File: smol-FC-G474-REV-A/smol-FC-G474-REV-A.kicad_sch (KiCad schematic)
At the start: 0 parts

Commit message: Schematic update
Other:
- added sheet Sensors & IC's (sens%IC.kicad_sch)
- sheet MCU ports: added ADC_CURR, AUX, Buzzer, CC, I2C3_SCL, I2C3_SDA, I2C4_SCL (BARO), I2C4_SDA (BARO), IMU_IRQ, LED, M1, M2, M3, M4, RX1, RX2 (VTX), RX3 (ELRS), RX4 (GPS), RX5 (TEL), SPI1_CS (OSD), SPI1_MISO (OSD), SPI1_MOSI (OSD), SPI1_SCK (OSD), SPI2_CS (IMU), SPI2_MISO (IMU), SPI2_MOSI (IMU), SPI2_SCK (IMU), SPI3_CS (Blackbox), SPI3_MISO (Blackbox), SPI3_MOSI (Blackbox), SPI3_SCK (Blackbox), TX1, TX2 (VTX), TX3 (ELRS), TX4 (GPS), TX5 (TEL); removed none

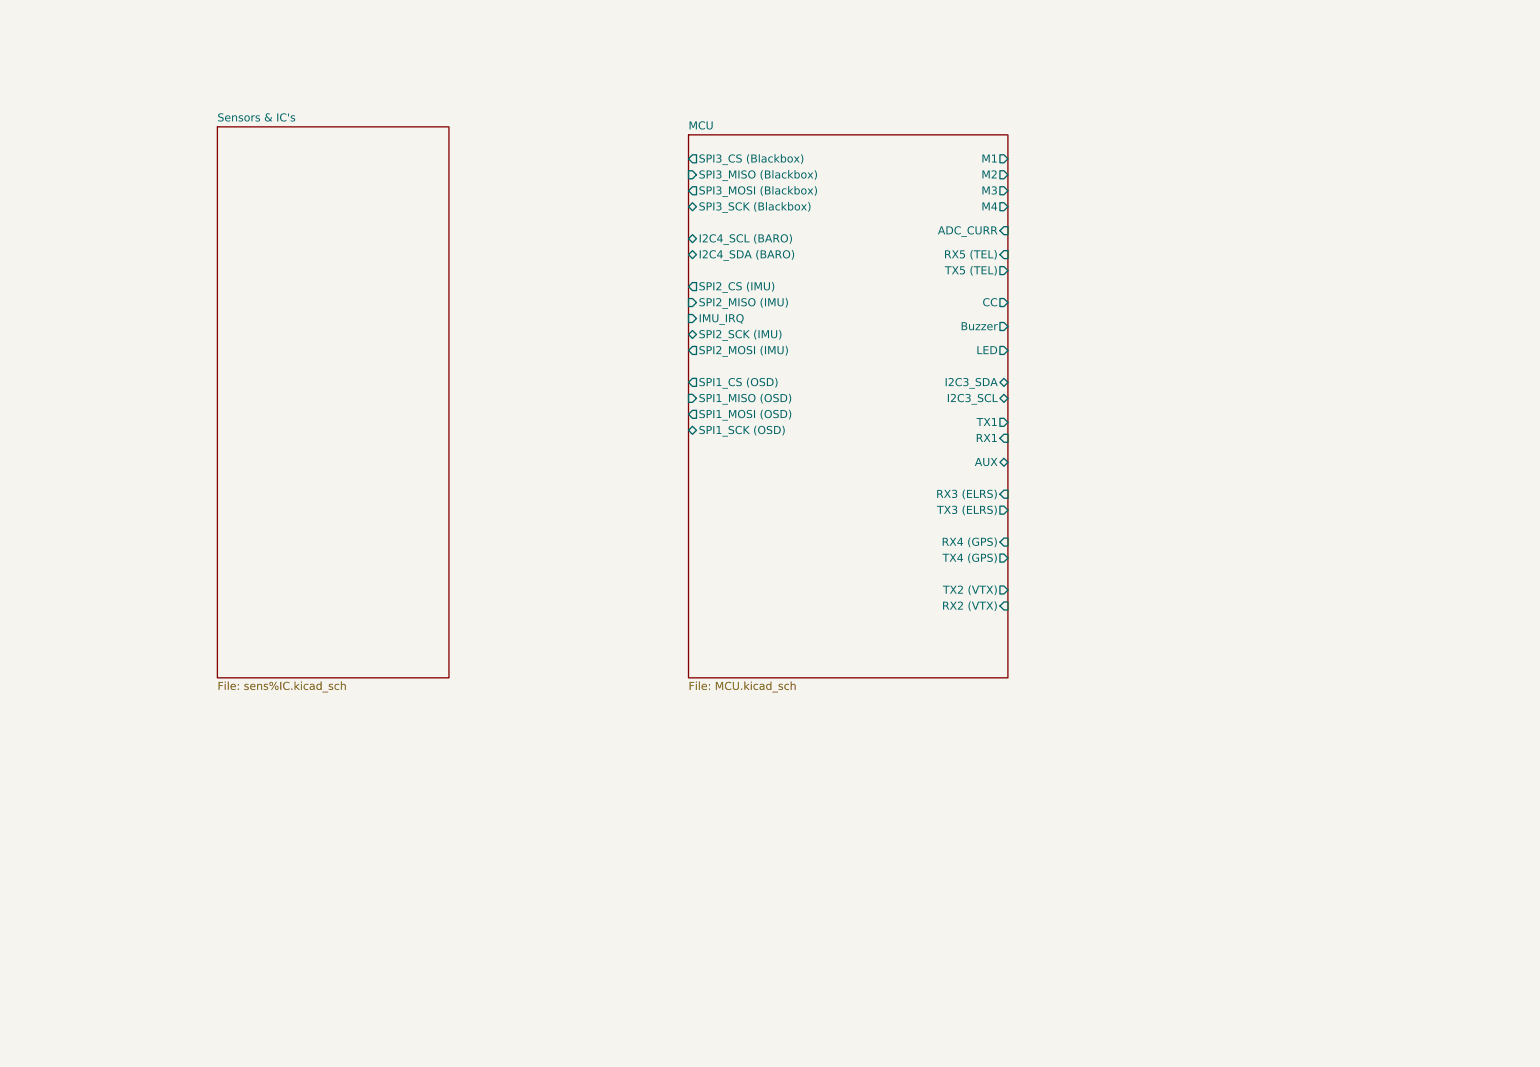
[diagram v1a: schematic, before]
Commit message: Added whole new schematic (sensors, OSD, Blackbox), changed text in cubemx
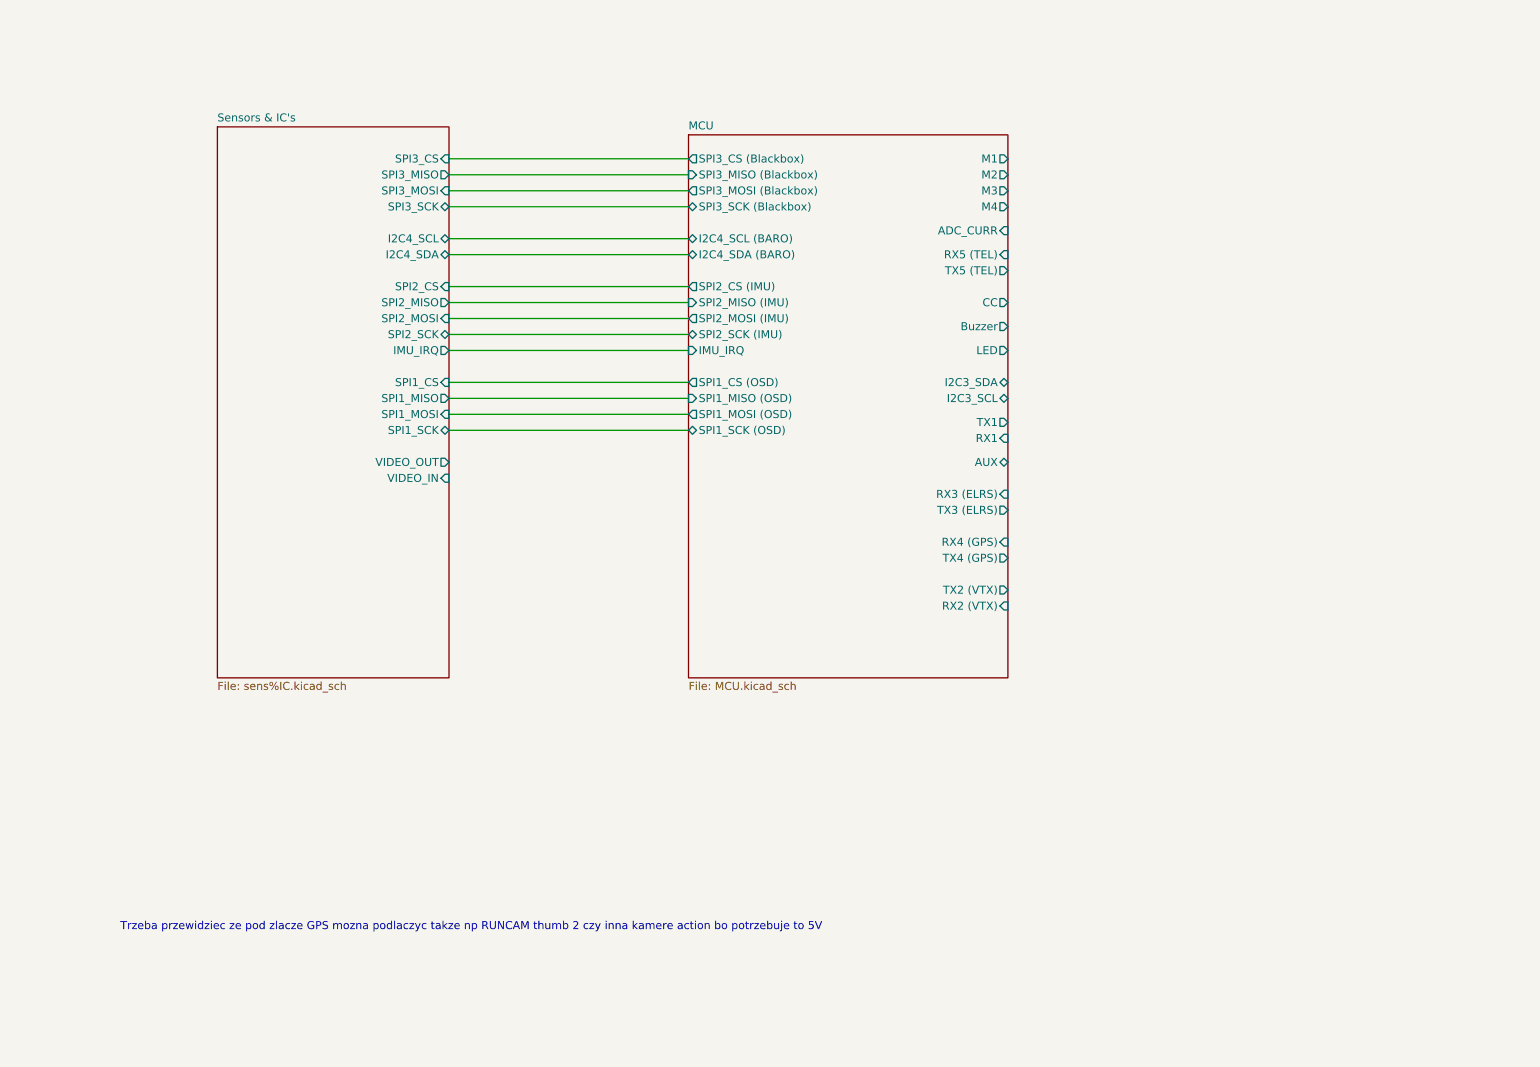
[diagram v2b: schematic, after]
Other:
- sheet Sensors & IC's ports: added I2C4_SCL, I2C4_SDA, IMU_IRQ, SPI1_CS, SPI1_MISO, SPI1_MOSI, SPI1_SCK, SPI2_CS, SPI2_MISO, SPI2_MOSI, SPI2_SCK, SPI3_CS, SPI3_MISO, SPI3_MOSI, SPI3_SCK, VIDEO_IN, VIDEO_OUT; removed none
- note added: "Trzeba przewidziec ze pod zlacze GPS mozna podlaczyc takze np RUNCAM thumb 2 czy inna kamere action bo potrzebuje to 5V"

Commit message: complete connectors layout and initialize buck converter section. Added buck docs in /docs.
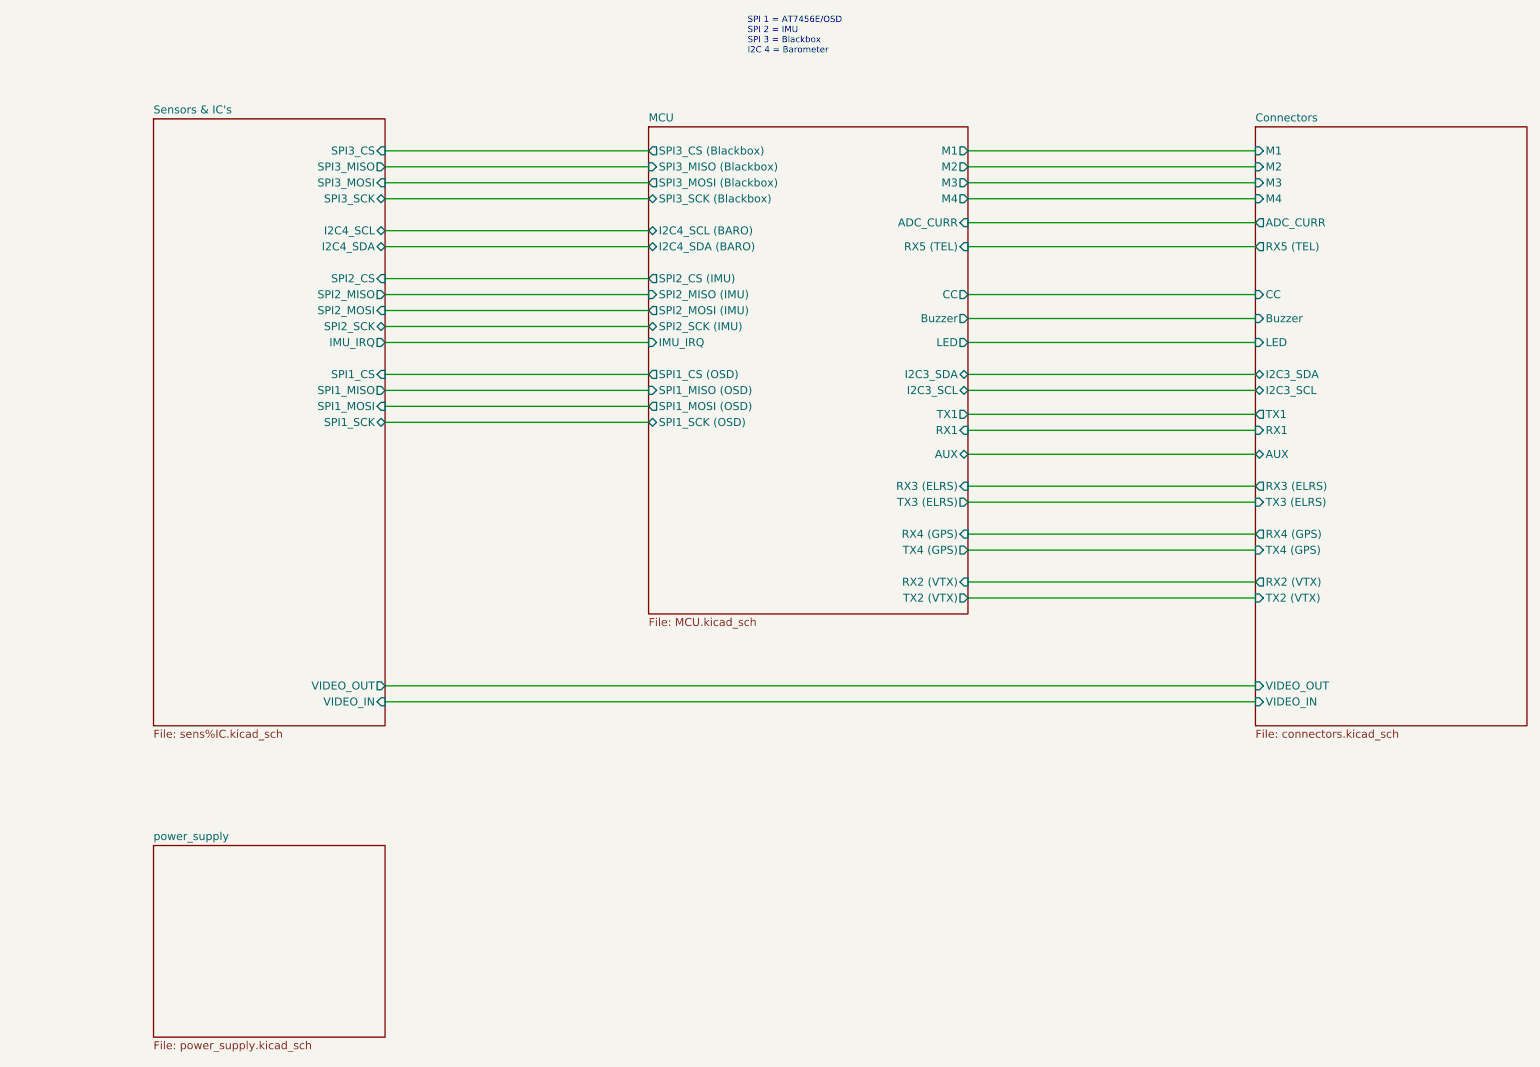
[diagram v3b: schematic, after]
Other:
- added sheet Connectors (connectors.kicad_sch)
- added sheet power_supply (power_supply.kicad_sch)
- sheet MCU ports: added none; removed TX5 (TEL)
- note added: "SPI 1 = AT7456E/OSD SPI 2 = IMU SPI 3 = Blackbox I2C 4 = Barometer"
- note removed: "Trzeba przewidziec ze pod zlacze GPS mozna podlaczyc takze np RUNCAM thumb 2 czy inna kamere action bo potrzebuje to 5V"

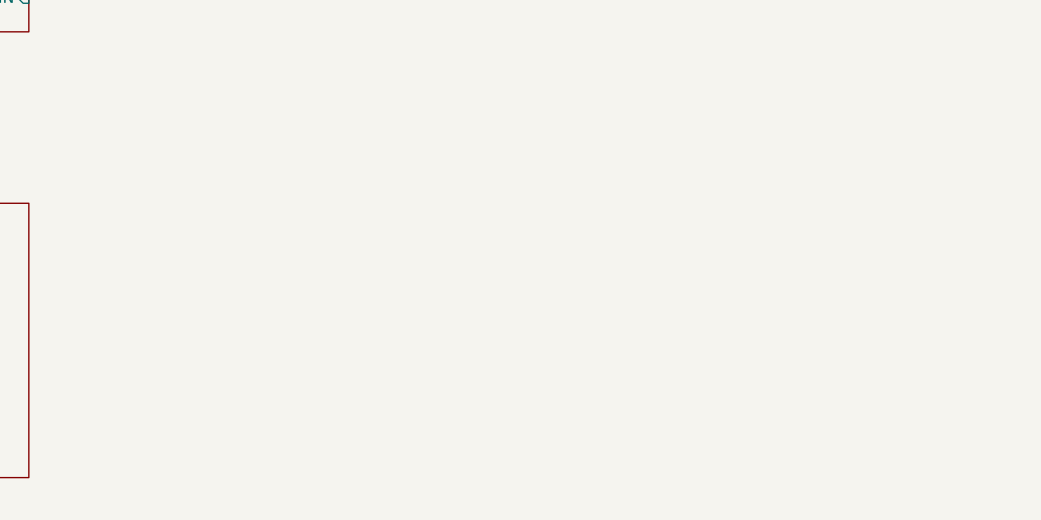
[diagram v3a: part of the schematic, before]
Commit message: Attached footprints and finalized schematic.
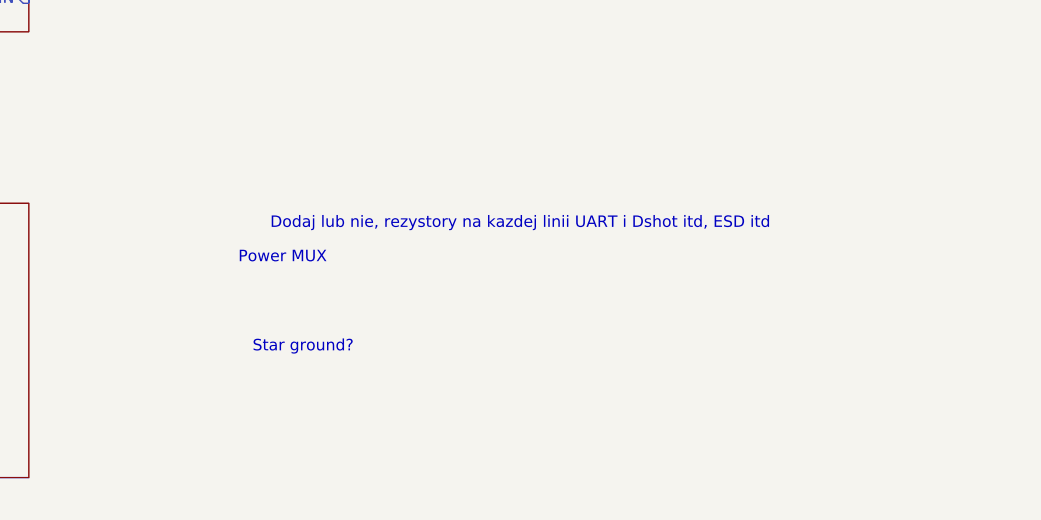
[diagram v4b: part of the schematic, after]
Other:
- note added: "Dodaj lub nie, rezystory na kazdej linii UART i Dshot itd, ESD itd"
- note added: "Power MUX"
- note added: "Star ground?"
- title: smol-FC-G474 -> smol-FC-G474-REV-A
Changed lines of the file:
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@@
 	(paper "A4")
 	(title_block
-		(title "smol-FC-G474")
-		(date "2026-05-31")
-		(rev "0.7.0")
+		(title "smol-FC-G474-REV-A")
+		(date "2026-06-05")
+		(rev "0.9.3")
 		(company "Daniel Plewa")
 		(comment 1 "License: CERN-OHL-W v2")
 		(comment 2 "GitHub: https://github.com/Def12345678/smol-FC-G474-REV-A")
-		(comment 3 "BEC 5A/2A, 10V/2A | Baro, OSD Chip and 16MB blackbox")
+		(comment 3 "BEC 5A/3A, 10V/3A | Baro, OSD Chip and 16MB blackbox")
 		(comment 4 "Open source flight controller on STM32G4, 20x20 3.5mm hole")
 	)
+	(text "Dodaj lub nie, rezystory na kazdej linii UART i Dshot itd, ESD itd"
+		(exclude_from_sim no)
+		(at 133.35 155.956 0)
+		(effects
+			(font
+				(size 1.27 1.27)
+			)
+		)
+	)
+	(text "Power MUX"
+		(exclude_from_sim no)
+		(at 106.934 159.766 0)
+		(effects
+			(font
+				(size 1.27 1.27)
+			)
+		)
+	)
+	(text "Star ground?"
+		(exclude_from_sim no)
+		(at 109.22 169.672 0)
+		(effects
+			(font
+				(size 1.27 1.27)
+			)
+		)
+	)
 	(text "SPI 1 = AT7456E/OSD\nSPI 2 = IMU\nSPI 3 = Blackbox\nI2C 4 = Barometer"

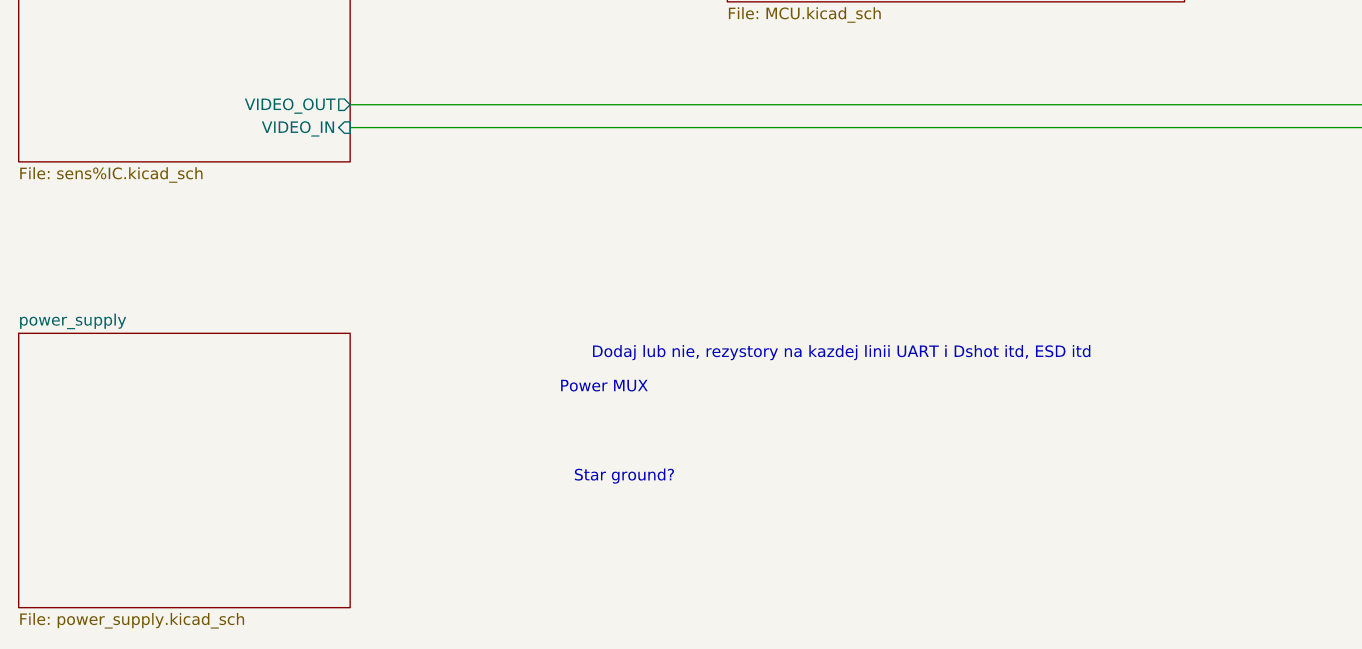
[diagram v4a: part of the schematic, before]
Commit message: Finalized schematic, added power mux
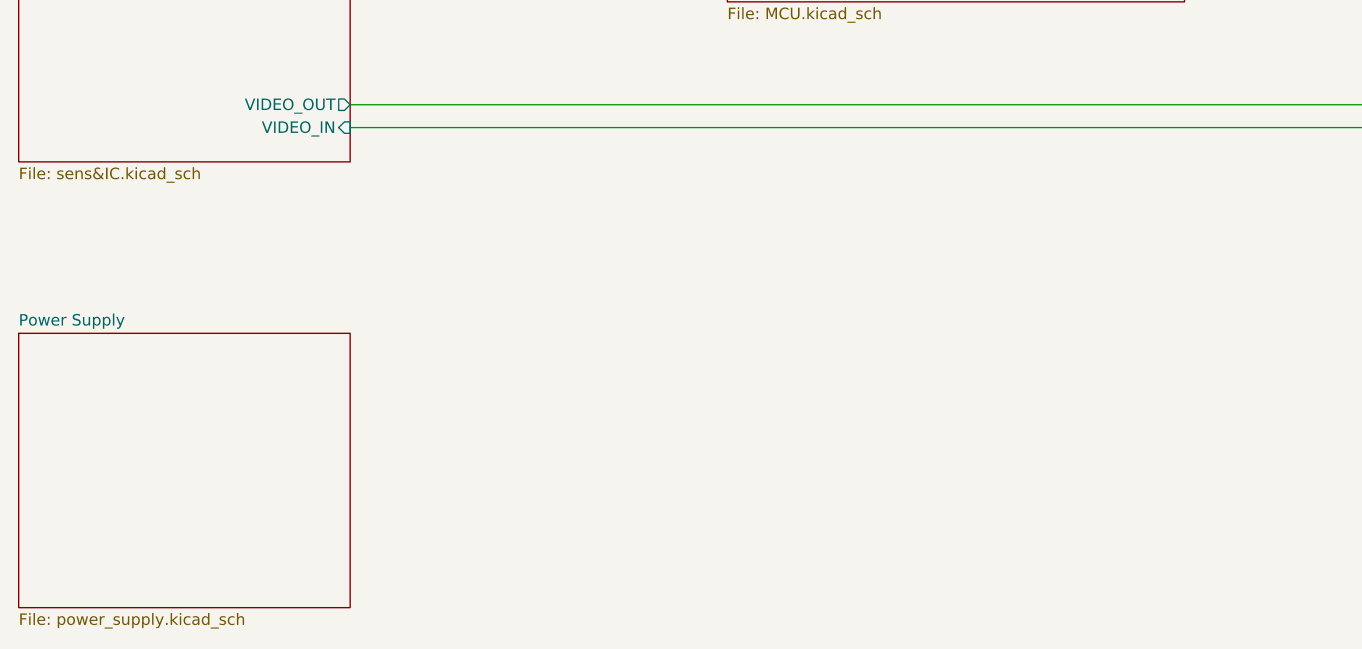
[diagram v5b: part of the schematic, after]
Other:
- sheet power_supply renamed Power Supply
- sheet Sensors & IC's: file sens%IC.kicad_sch -> sens&IC.kicad_sch
- note removed: "Dodaj lub nie, rezystory na kazdej linii UART i Dshot itd, ESD itd"
- note removed: "Power MUX"
- note removed: "Star ground?"
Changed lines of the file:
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@@
 		(comment 1 "License: CERN-OHL-W v2")
 		(comment 2 "GitHub: https://github.com/Def12345678/smol-FC-G474-REV-A")
-		(comment 3 "BEC 5A/3A, 10V/3A | Baro, OSD Chip and 16MB blackbox")
+		(comment 3 "BEC 5A/3A, 9V/3A | Baro, OSD Chip and 16MB blackbox")
 		(comment 4 "Open source flight controller on STM32G4, 20x20 3.5mm hole")
-	)
-	(text "Dodaj lub nie, rezystory na kazdej linii UART i Dshot itd, ESD itd"
-		(exclude_from_sim no)
-		(at 133.35 155.956 0)
-		(effects
-			(font
-				(size 1.27 1.27)
-			)
-		)
-	)
-	(text "Power MUX"
-		(exclude_from_sim no)
-		(at 106.934 159.766 0)
-		(effects
-			(font
-				(size 1.27 1.27)
-			)
-		)
-	)
-	(text "Star ground?"
-		(exclude_from_sim no)
-		(at 109.22 169.672 0)
-		(effects
-			(font
-				(size 1.27 1.27)
-			)
-		)
 	)
 	(text "SPI 1 = AT7456E/OSD\nSPI 2 = IMU\nSPI 3 = Blackbox\nI2C 4 = Barometer"
@@
 			(color 255 229 191 1)
 		)
-		(property "Sheetname" "power_supply"
+		(property "Sheetname" "Power Supply"
 			(at 41.91 152.9584 0)
 			(show_name no)
@@
 			)
 		)
-		(property "Sheetfile" "sens%IC.kicad_sch"
+		(property "Sheetfile" "sens&IC.kicad_sch"
 			(at 41.91 135.2046 0)
 			(show_name no)

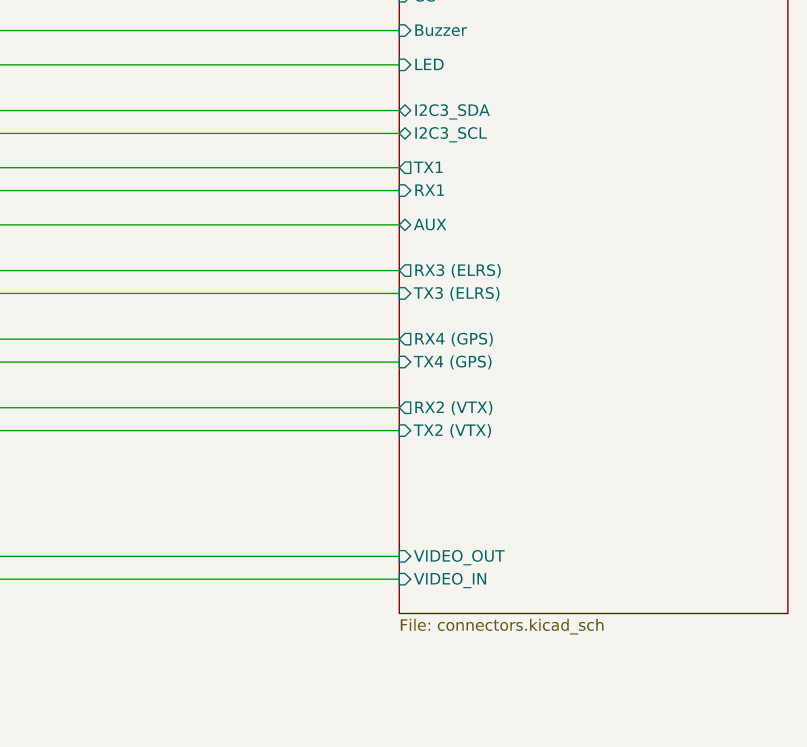
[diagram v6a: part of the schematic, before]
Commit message: changed size of cap on buck's
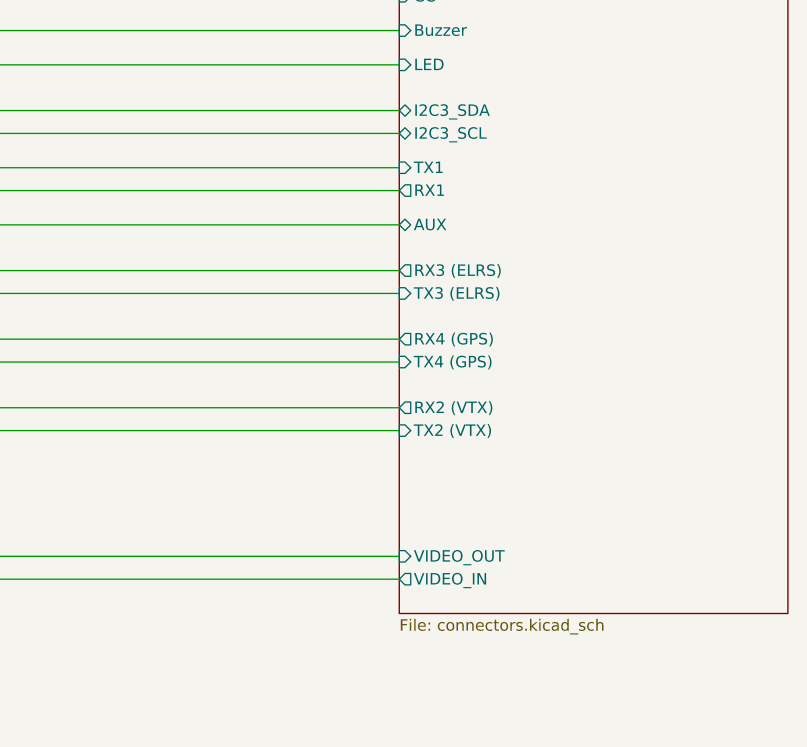
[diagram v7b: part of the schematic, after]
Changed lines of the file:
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@@
 			)
 		)
-		(pin "TX1" output
+		(pin "TX1" input
 			(at 217.17 85.09 180)
 			(effects
@@
 			)
 		)
-		(pin "RX1" input
+		(pin "RX1" output
 			(at 217.17 87.63 180)
 			(effects
@@
 			)
 		)
-		(pin "VIDEO_IN" input
+		(pin "VIDEO_IN" output
 			(at 217.17 130.81 180)
 			(effects
